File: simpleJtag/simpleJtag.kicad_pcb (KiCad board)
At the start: 2 copper layers, 35.9 x 20 mm, 20 parts, among them J1 Conn_02x05_Odd_Even, P1 USB_C_Plug, U1 AP7333-33SRG-7, U2 CH552T

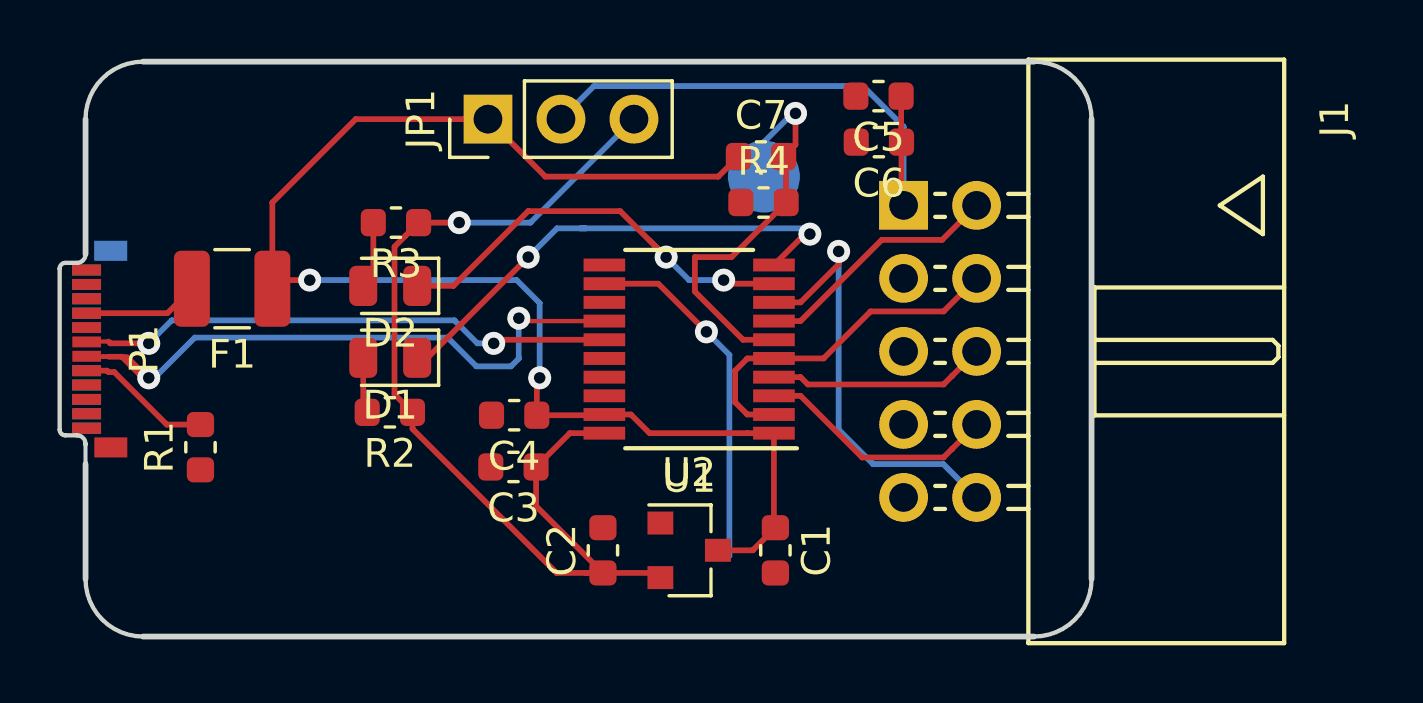
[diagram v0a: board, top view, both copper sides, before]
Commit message: swapping USBC plug to USBC socket
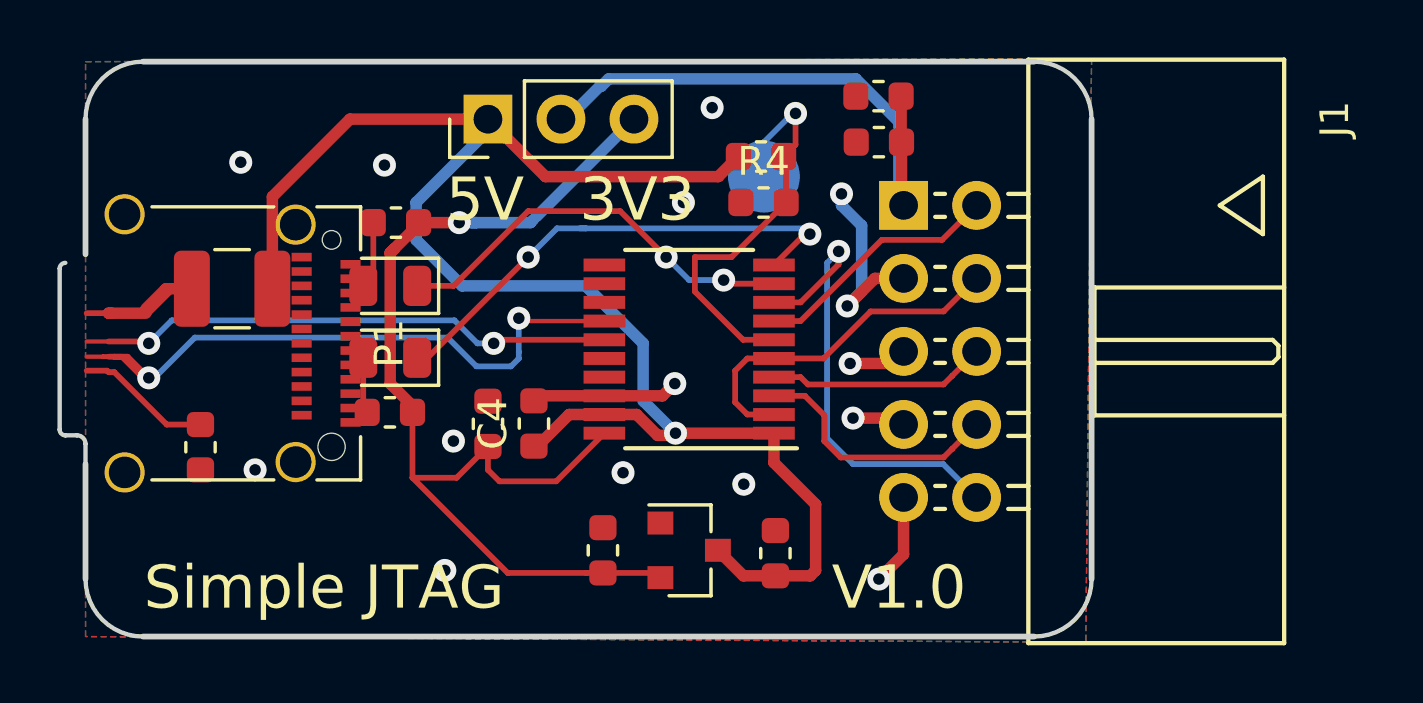
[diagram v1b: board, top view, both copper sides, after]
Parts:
- P1: footprint Connector_USB:USB_C_Plug_Molex_105444 -> Connector_USB:USB_C_Receptacle_Amphenol_12401610E4-2A_CircularHoles
- moved P1 4.20 mm to (137.2, 62.8), turned to 270 degrees
- moved C3 1.74 mm to (147.0, 65.6), turned to 90 degrees
- moved C4 0.75 mm to (148.6, 65.6), turned to 90 degrees
- moved C1 0.10 mm to (157.0, 70.1), turned to 90 degrees
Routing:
- net GND: track 0.00 -> 19.0 mm, vias 0 -> 15
- net Net-(TP3-Pad1): track 12.4 -> 0.00 mm, vias 1 -> 0
- net VBUS: track 49.4 -> 58.3 mm, vias 2 -> 1
- net +3V3: track 35.0 -> 39.5 mm
- net Net-(F1-Pad2): track 4.01 -> 6.10 mm
- net Net-(D2-Pad1): track 15.4 -> 14.5 mm
- net /J_RESET: track 15.2 -> 16.0 mm
- net /TDI: track 8.41 -> 8.94 mm
- added copper zone on B.Cu, net GND
- added copper zone on F.Cu, net GND
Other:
- outline, holes or cut-outs redrawn
- net class vbus added: clearance 0.2, trace_width 0.4, via_dia 0.8, via_drill 0.4
- board text added: "3V3"
- board text added: "5V"
- board text added: "Simple JTAG"
- board text added: "V1.0"

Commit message: end of day sync
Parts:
- P1: footprint Connector_USB:USB_C_Receptacle_Amphenol_12401610E4-2A_CircularHoles -> footprint:usbc_16pos_lugged_allsmt
- moved R1 12.6 mm to (142.7, 55.2), turned to 180 degrees
- moved F1 10.1 mm to (143.4, 69.5)
- moved D1 9.86 mm to (135.9, 69.5), turned to 0 degrees
- moved D2 9.27 mm to (136.0, 55.5), turned to 0 degrees
- moved R2 6.08 mm to (139.3, 69.5)
- moved R3 5.54 mm to (139.2, 55.5)
- moved P1 0.61 mm to (137.5, 62.3)
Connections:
- P1 pad B6: (no net) -> /USBD+
- P1 pad B7: (no net) -> /USBD-
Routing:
- net +3V3: track 39.5 -> 56.2 mm, vias 1 -> 0
- net Net-(F1-Pad2): track 6.10 -> 18.6 mm, vias 0 -> 2
- net /USBD+: track 23.8 -> 12.3 mm, vias 2 -> 0
- net Net-(D2-Pad1): track 14.5 -> 4.13 mm
- net Net-(D1-Pad1): track 17.5 -> 12.0 mm
- net Net-(P1-PadA5): track 4.74 -> 7.77 mm
- net Net-(D2-Pad2): track 2.34 -> 0.00 mm
- net GND: track 19.0 -> 21.2 mm, vias 15 -> 14
- net Net-(D1-Pad2): track 1.96 -> 0.00 mm
- net /USBD-: track 18.8 -> 17.9 mm
- net VBUS: track 58.3 -> 57.6 mm
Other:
- board size 35.9 x 20 mm -> 35 x 20 mm
- board text removed: "5V"

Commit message: end of day sync
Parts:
- added C8: 22pf, Capacitor_SMD:C_0603_1608Metric, F.Cu at (147.6, 57.6)
- added C9: 22pf, Capacitor_SMD:C_0603_1608Metric, F.Cu at (147.7, 63.3)
- added Y1: Crystal_GND24, Crystal:Crystal_SMD_3225-4Pin_3.2x2.5mm, F.Cu at (147.6, 60.5)
- moved D1 14.4 mm to (135.6, 55.1)
- moved R2 14.4 mm to (139.2, 55.1)
- moved D2 14.0 mm to (135.4, 69.5)
- moved R3 14.0 mm to (139.1, 69.5)
- moved U2 0.92 mm to (154.9, 63.0)
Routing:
- net Net-(D2-Pad1): track 4.13 -> 34.8 mm
- net Net-(D1-Pad1): track 12.0 -> 27.2 mm
- net Net-(C8-Pad1): track 0.00 -> 9.67 mm
- net GND: track 21.2 -> 26.8 mm, vias 14 -> 23
- net Net-(C9-Pad1): track 0.00 -> 5.59 mm
- net /USBD+: track 12.3 -> 17.1 mm, vias 0 -> 2
- net VBUS: track 57.6 -> 61.0 mm
- net Net-(F1-Pad2): track 18.6 -> 16.5 mm
- net Net-(D1-Pad2): track 0.00 -> 1.80 mm
- net Net-(D2-Pad2): track 0.00 -> 1.62 mm
- net /USBD-: track 17.9 -> 16.6 mm
- net /RESET: track 14.6 -> 13.6 mm, vias 1 -> 2
- net /TCK: track 12.4 -> 11.4 mm
- net /TDO: track 7.63 -> 6.71 mm
- net /TDI: track 8.94 -> 8.25 mm
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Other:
- net class USB removed
- rule trace_min: 0.15 -> 0.2

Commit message: Routing v1 complete drc done ready for FAB
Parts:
- added G***: LOGO, silks:back, B.Cu at (150.4, 62.9)
- added G***: LOGO, silks:front, F.Cu at (150.3, 71.2)
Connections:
- P1 pad A8: Net-(P1-PadA8) -> (no net)
- P1 pad B5: Net-(P1-PadB5) -> (no net)
- P1 pad B8: Net-(P1-PadB8) -> (no net)
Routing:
- net Net-(D2-Pad2): track 1.62 -> 2.20 mm
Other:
- board text removed: "3V3"
- board text removed: "Simple JTAG"
- board text removed: "V1.0"
